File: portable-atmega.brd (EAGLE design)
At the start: 49.7 x 42.7 mm, 35 parts

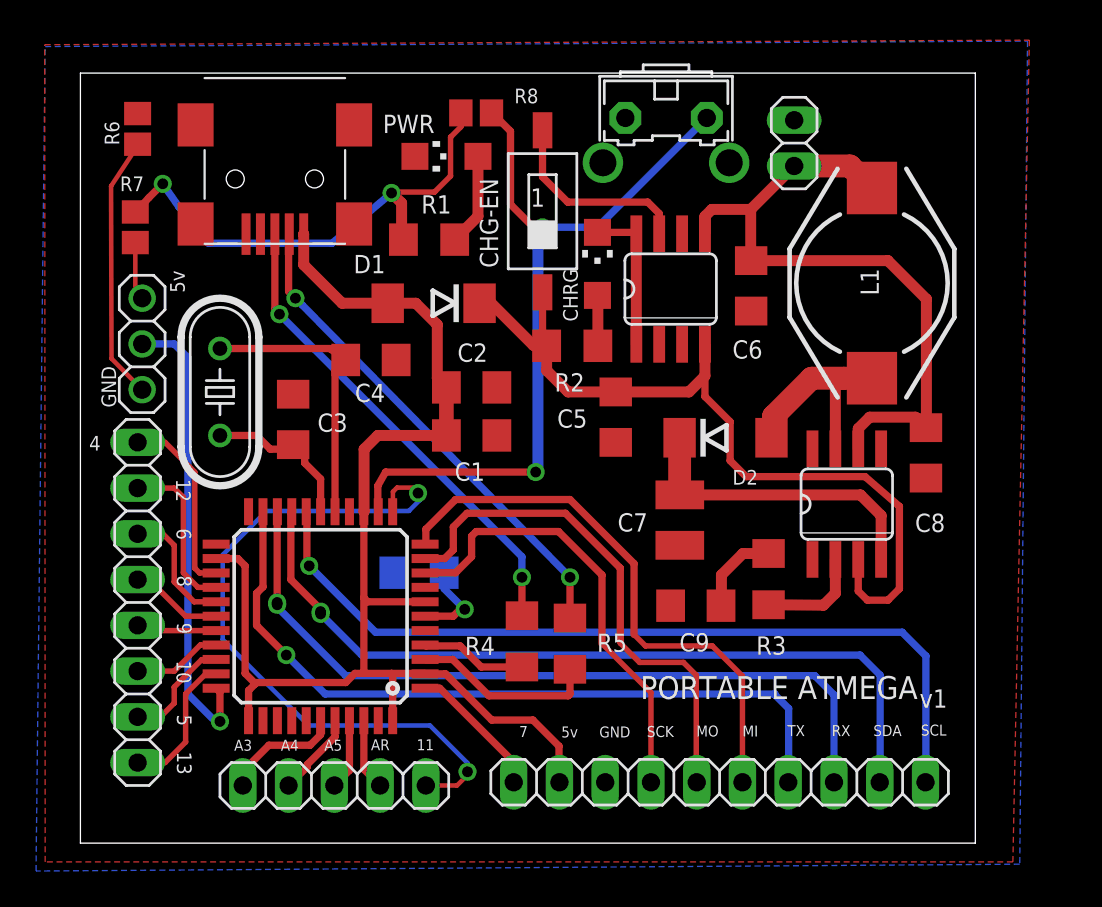
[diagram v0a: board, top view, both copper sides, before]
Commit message: Updated Schematic and BRD
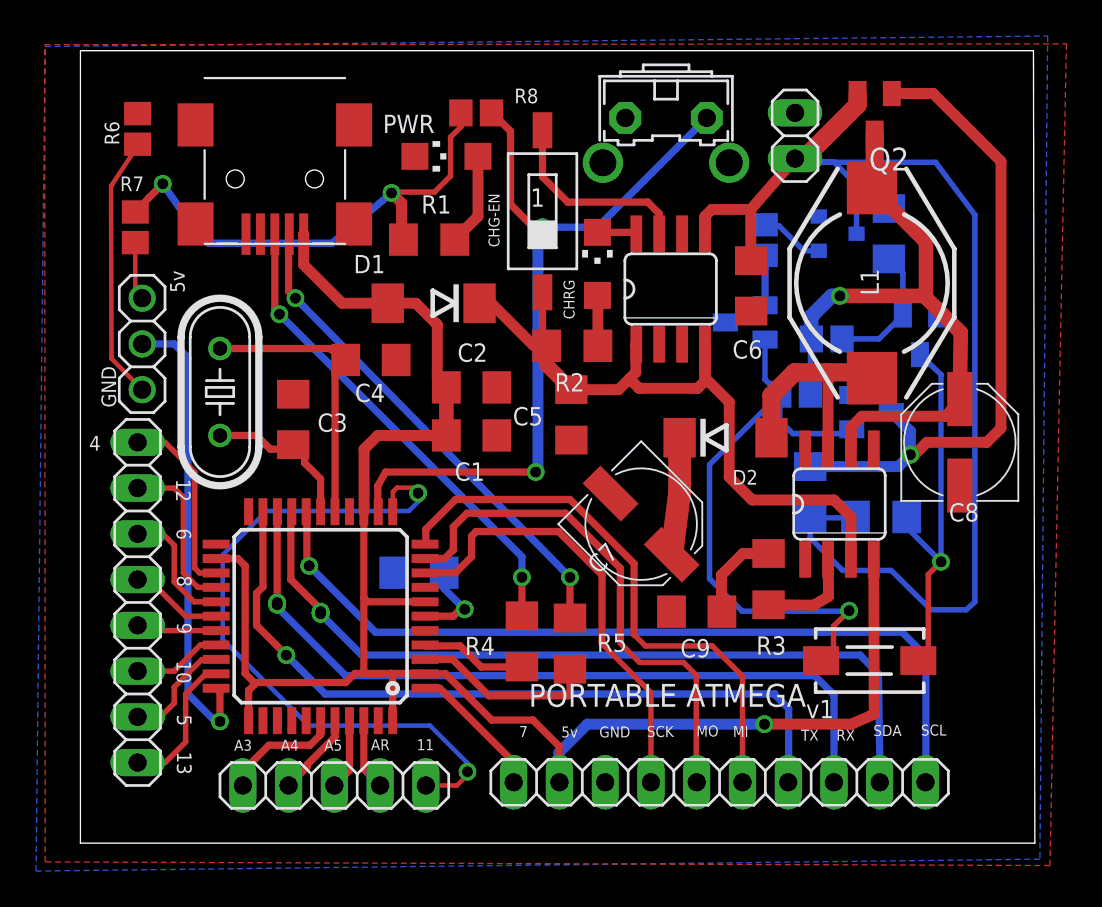
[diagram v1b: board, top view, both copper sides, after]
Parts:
- added C11: 10uf, resistor:C1206
- added Q2: BSS84, transistor-small-signal:SOT23
- added Q3: MMBT3906LT1SMD, transistor-pnp:SOT23-BEC
- added Q4, Q5: (no value), semicon-smd-ipc:SOT23
- added R10, R12: 10k, resistor:R1206
- added R11: 100k, solar3-1:R0805
- added R13, R9: 10k, solar3-1:R0805
- added S2: DTSM-3, switch-tact:DTSM-3
- added U$3: TC54, microchip:SOT23-3
- C7: device resistor:C3225 -> resistor:PANASONIC_D
- C8: device resistor:C1206 -> resistor:PANASONIC_D
- moved C5 2.47 mm to (27.4, 23.9)
- moved C7 2.16 mm to (31.3, 17.9), turned to 315 degrees
- moved C8 1.97 mm to (49.0, 22.4)
- moved JP1 0.41 mm to (39.9, 39.4)
- moved U$4 0.41 mm to (42.3, 19.0)
- moved C9 0.33 mm to (34.4, 13.0)
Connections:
- new net IN2: C8.+, L1.2, Q2.3, R11.1, R9.1, U$4.6
- new net N$39: Q2.1, Q5.3, R10.2
- new net N$40: Q3.E, Q5.1, R9.2, S2.1
- new net N$42: C11.1, Q4.1, R11.2
- new net N$43: Q4.3, R12.2, S2.2
- new net N$46: R13.2, U$3.1
- new net N$47: Q3.B, R13.1
- net +5V: now also U$4.4
- net BAT+: now also Q2.2, R10.1, R12.1, U$3.3; no longer C8.2, L1.2, U$4.6
- net GND: now also C11.2, C7.-, C8.-, Q3.C, Q4.2, Q5.2, U$3.2; no longer C7.2, C8.1
- net IN: now also U$1.1
- net N$4: no longer U$1.1
- net OUTPUT: now also C7.+; no longer C7.1, U$4.4
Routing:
- net IN2: track 0.00 -> 38.2 mm, vias 0 -> 1
- net N$39: track 0.00 -> 37.0 mm, vias 0 -> 1
- net N$40: track 0.00 -> 34.0 mm, vias 0 -> 1
- net BAT+: track 37.9 -> 71.9 mm
- net +5V: track 100.0 -> 128.5 mm, vias 2 -> 3
- net N$43: track 0.00 -> 21.7 mm, vias 0 -> 1
- net OUTPUT: track 17.5 -> 9.85 mm
- net N$42: track 0.00 -> 7.37 mm
- net IN: track 47.0 -> 40.7 mm
- net N$4: track 8.34 -> 2.19 mm
- net N$46: track 0.00 -> 3.61 mm
- net N$47: track 0.00 -> 2.77 mm
- net N$8: track 11.7 -> 12.8 mm
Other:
- board size 49.7 x 42.7 mm -> 53 x 44 mm
